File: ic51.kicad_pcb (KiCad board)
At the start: 2 copper layers, 80 x 80 mm, 5 parts, among them J1 Conn_02x18_Odd_Even, J2 Conn_02x18_Odd_Even, J3 Conn_02x18_Odd_Even, J4 Conn_02x18_Odd_Even, U1 ic51-1444-schem

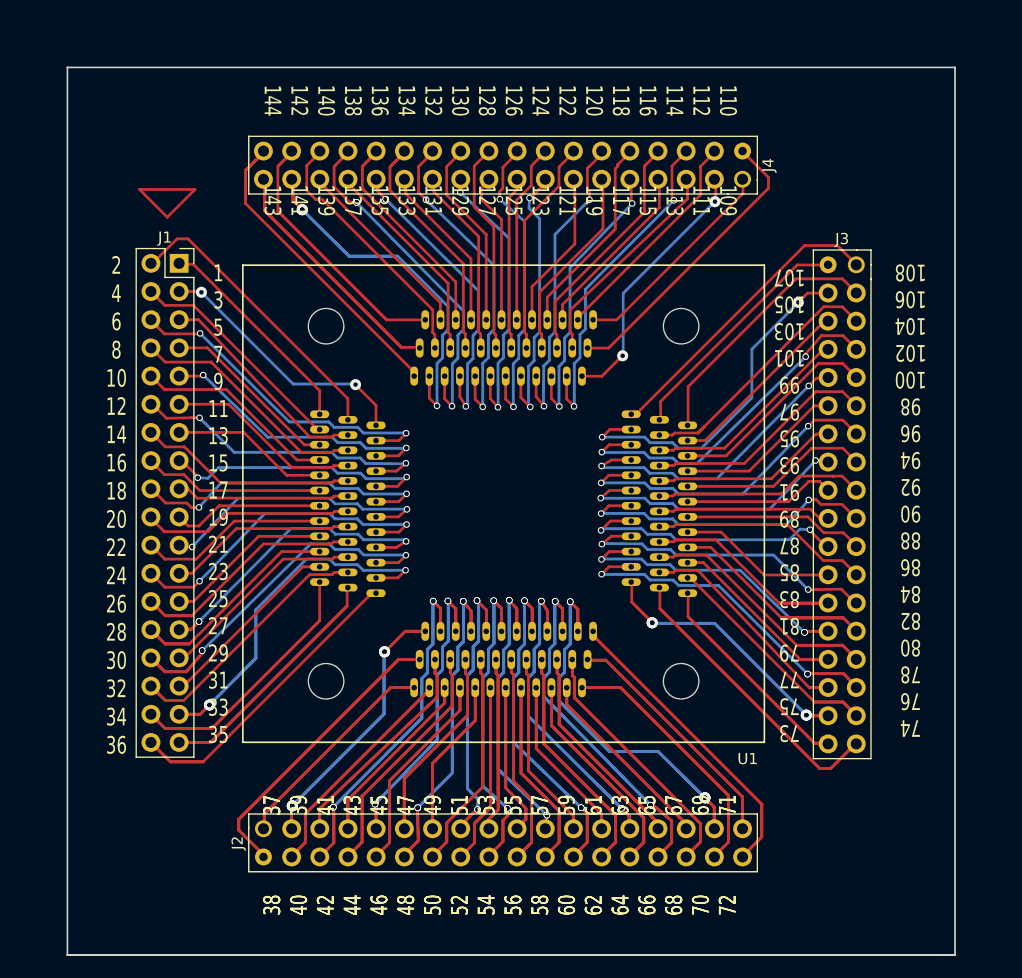
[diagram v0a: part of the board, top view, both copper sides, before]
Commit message: decrease font size og text in F.silk layer
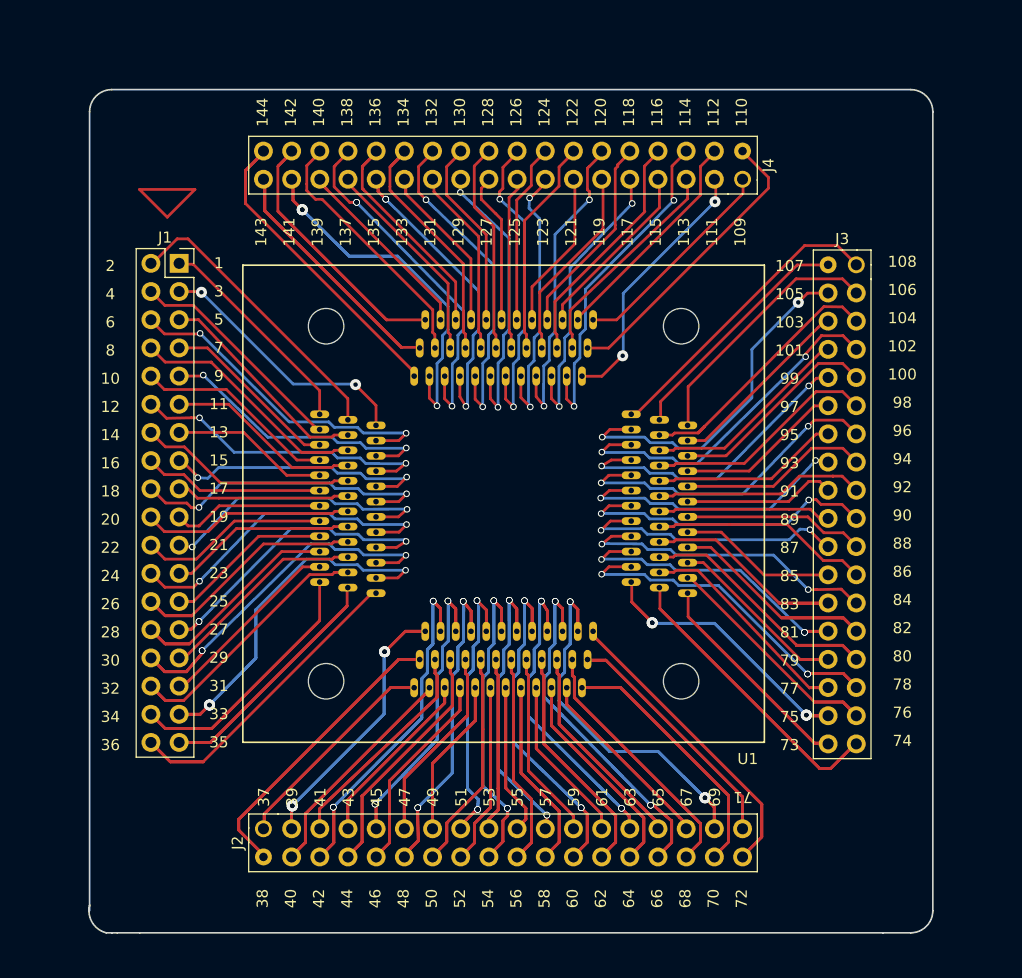
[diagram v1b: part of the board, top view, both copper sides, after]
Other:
- board size 80 x 80 mm -> 76.1 x 76 mm
- board text added: "10"
- board text added: "100"
- board text added: "101"
- board text added: "102"
- board text added: "103"
- board text added: "104"
- board text added: "105"
- board text added: "106"
- board text added: "107"
- board text added: "108"
- board text added: "109"
- board text added: "11"
- board text added: "110"
- board text added: "111"
- board text added: "112"
- board text added: "113"
- board text added: "114"
- board text added: "115"
- board text added: "116"
- board text added: "117"
- board text added: "118"
- board text added: "119"
- board text added: "12"
- board text added: "120"
- board text added: "121"
- board text added: "122"
- board text added: "123"
- board text added: "124"
- board text added: "125"
- board text added: "126"
- board text added: "127"
- board text added: "128"
- board text added: "129"
- board text added: "13"
- board text added: "130"
- board text added: "131"
- board text added: "132"
- board text added: "133"
- board text added: "134"
- board text added: "135"
- board text added: "136"
- board text added: "137"
- board text added: "138"
- board text added: "139"
- board text added: "14"
- board text added: "140"
- board text added: "141"
- board text added: "142"
- board text added: "143"
- board text added: "144"
- board text added: "15"
- board text added: "16"
- board text added: "17"
- board text added: "18"
- board text added: "19"
- board text added: "2"
- board text added: "20"
- board text added: "21"
- board text added: "22"
- board text added: "23"
- board text added: "24"
- board text added: "25"
- board text added: "26"
- board text added: "27"
- board text added: "28"
- board text added: "29"
- board text added: "3"
- board text added: "30"
- board text added: "31"
- board text added: "32"
- board text added: "33"
- board text added: "34"
- board text added: "35"
- board text added: "36"
- board text added: "37"
- board text added: "38"
- board text added: "39"
- board text added: "4"
- board text added: "40"
- board text added: "41"
- board text added: "42"
- board text added: "43"
- board text added: "44"
- board text added: "45"
- board text added: "46"
- board text added: "47"
- board text added: "48"
- board text added: "49"
- board text added: "5"
- board text added: "50"
- board text added: "51"
- board text added: "52"
- board text added: "53"
- board text added: "54"
- board text added: "55"
- board text added: "56"
- board text added: "57"
- board text added: "58"
- board text added: "59"
- board text added: "6"
- board text added: "60"
- board text added: "61"
- board text added: "62"
- board text added: "63"
- board text added: "64"
- board text added: "65"
- board text added: "66"
- board text added: "67"
- board text added: "68"
- board text added: "69"
- board text added: "7"
- board text added: "70"
- board text added: "71"
- board text added: "72"
- board text added: "73"
- board text added: "74"
- board text added: "75"
- board text added: "76"
- board text added: "77"
- board text added: "78"
- board text added: "79"
- board text added: "8"
- board text added: "80"
- board text added: "81"
- board text added: "82"
- board text added: "83"
- board text added: "84"
- board text added: "85"
- board text added: "86"
- board text added: "87"
- board text added: "88"
- board text added: "89"
- board text added: "9"
- board text added: "90"
- board text added: "91"
- board text added: "92"
- board text added: "93"
- board text added: "94"
- board text added: "95"
- board text added: "96"
- board text added: "97"
- board text added: "98"
- board text added: "99"
- board text removed: "1 3 5 7 9 11 13 15 17 19 21 23 25 27 29 31 33 35"
- board text removed: "109 111 113 115 117 119 121 123 125 127 129 131 133 135 137 139 141 143"
- board text removed: "110 112 114 116 118 120 122 124 126 128 130 132 134 136 138 140 142 144"
- board text removed: "2 4 6 8 10 12 14 16 18 20 22 24 26 28 30 32 34 36"
- board text removed: "37 39 41 43 45 47 49 51 53 55 57 59 61 63 65 67 69 71"
- board text removed: "38 40 42 44 46 48 50 52 54 56 58 60 62 64 66 68 70 72"
- board text removed: "73 75 77 79 81 83 85 87 89 91 93 95 97 99 101 103 105 107"
- board text removed: "74 76 78 80 82 84 86 88 90 92 94 96 98 100 102 104 106 108"

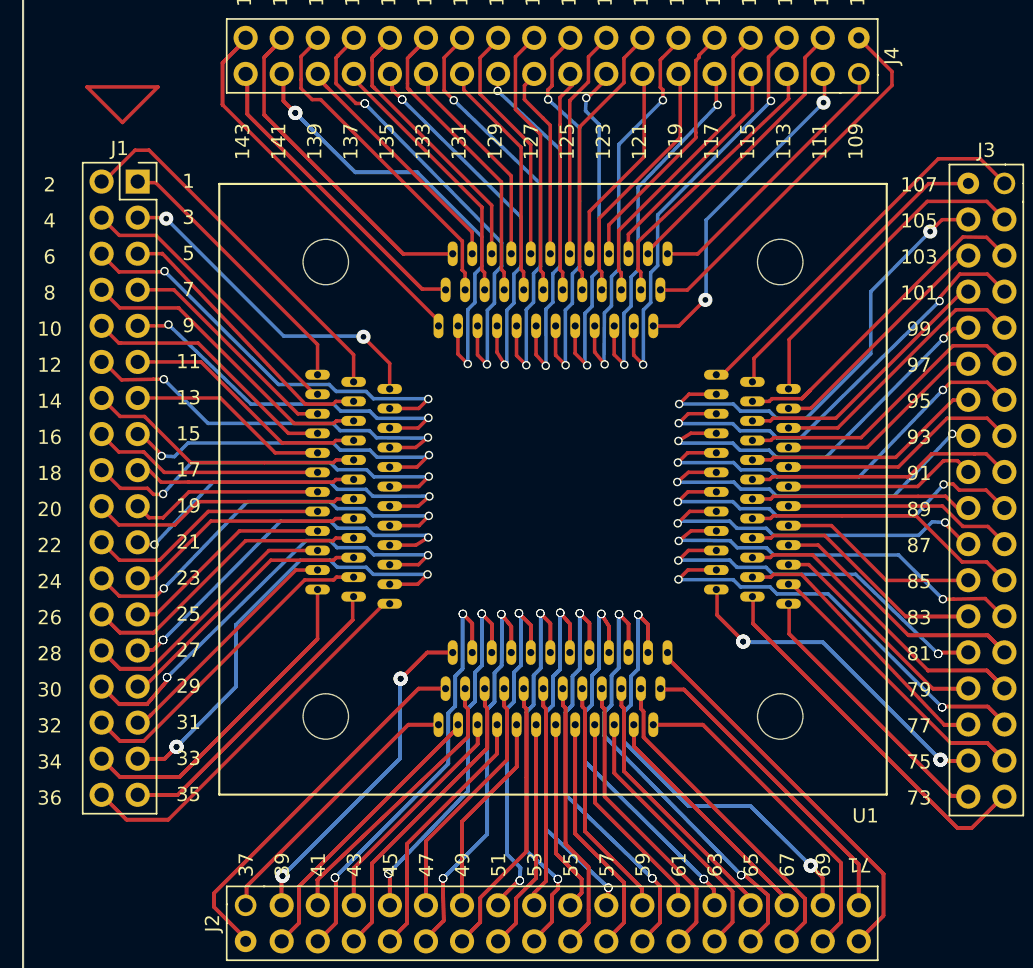
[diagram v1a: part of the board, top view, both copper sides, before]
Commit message: unify all vias to 0.6mm, decrease the size of the triangle
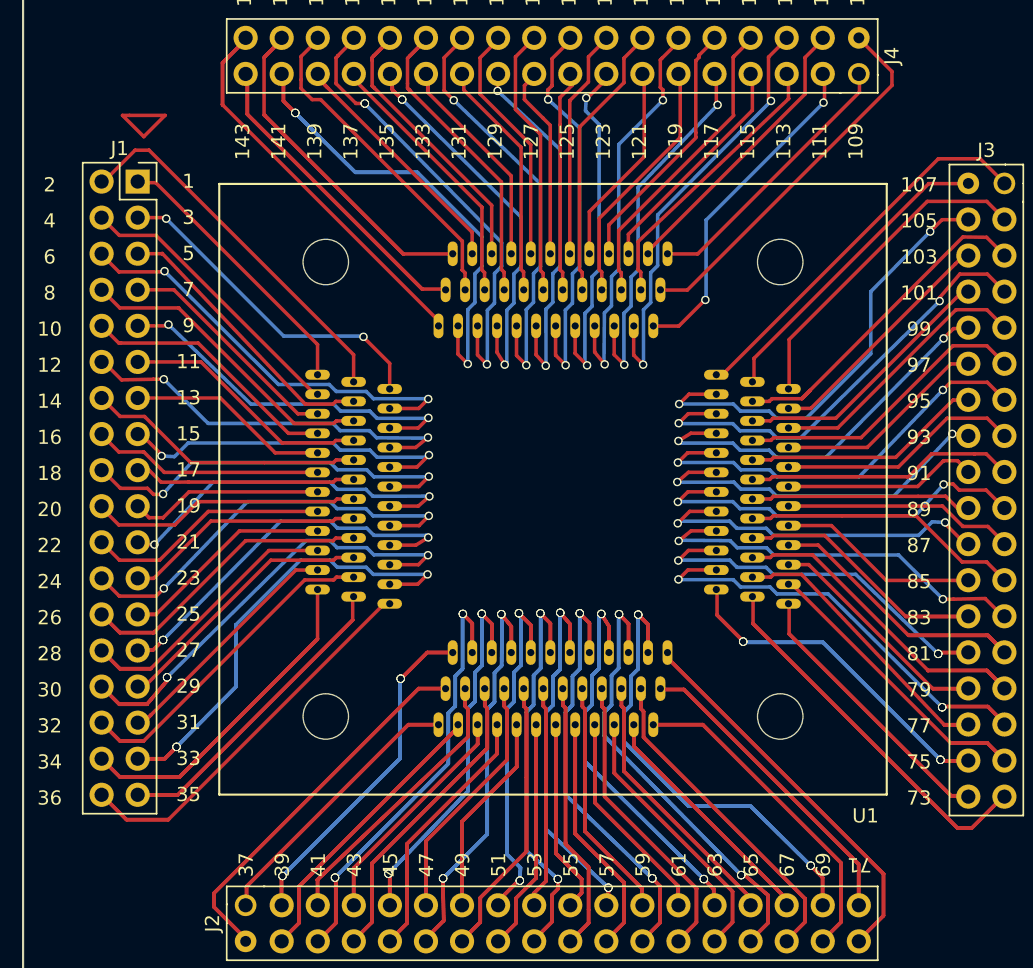
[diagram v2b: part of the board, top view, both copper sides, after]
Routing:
- net (no net): track 13.0 -> 8.14 mm
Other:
- net class Default: via_dia 1 -> 0.6
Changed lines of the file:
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@@
     (links 144)
     (no_connects 0)
-    (area 108.863446 56.424999 185.075001 132.575001)
+    (area -111.414286 -111.414286 213.909502 133.042382)
     (thickness 1.6)
     (drawings 159)
-    (tracks 1567)
+    (tracks 1568)
     (zones 0)
     (modules 5)
@@
     (segment_width 0.2)
     (edge_width 0.15)
-    (via_size 1)
+    (via_size 0.6)
     (via_drill 0.4)
     (via_min_size 0.4)
@@
     (clearance 0.2)
     (trace_width 0.25)
-    (via_dia 1)
+    (via_dia 0.6)
     (via_drill 0.4)
     (uvia_dia 0.3)
@@
     (effects (font (size 1.5 1.5) (thickness 0.3)))
   )
-  (segment (start 113.5 65.5) (end 118.5 65.5) (width 0.25) (layer F.Cu) (net 0))
-  (segment (start 116 68) (end 113.5 65.5) (width 0.25) (layer F.Cu) (net 0))
-  (segment (start 118.5 65.5) (end 116 68) (width 0.25) (layer F.Cu) (net 0))
+  (segment (start 116.5 67.5) (end 119 67.5) (width 0.25) (layer F.Cu) (net 0))
+  (segment (start 116 67.5) (end 116.5 67.5) (width 0.25) (layer F.Cu) (net 0))
+  (segment (start 117.5 69) (end 116 67.5) (width 0.25) (layer F.Cu) (net 0))
+  (segment (start 119 67.5) (end 117.5 69) (width 0.25) (layer F.Cu) (net 0))
   (segment (start 213.5845 97.840999) (end 213.5845 98.3535) (width 0.25) (layer F.Cu) (net 0))
   (segment (start 213.5845 98.2235) (end 213.5845 97.840999) (width 0.25) (layer F.Cu) (net 0))
@@
   (segment (start 119.01 74.7) (end 116.88 74.7) (width 0.25) (layer F.Cu) (net 3))
   (segment (start 119.08 74.77) (end 119.01 74.7) (width 0.25) (layer F.Cu) (net 3))
-  (via (at 119.08 74.77) (size 1) (drill 0.4) (layers F.Cu B.Cu) (net 3))
+  (via (at 119.08 74.77) (size 0.6) (drill 0.4) (layers F.Cu B.Cu) (net 3))
   (segment (start 127.35 83.04) (end 119.08 74.77) (width 0.25) (layer B.Cu) (net 3))
   (segment (start 132.92 83.04) (end 127.35 83.04) (width 0.25) (layer B.Cu) (net 3))
   (segment (start 132.97 83.09) (end 132.92 83.04) (width 0.25) (layer B.Cu) (net 3))
-  (via (at 132.97 83.09) (size 1) (drill 0.4) (layers F.Cu B.Cu) (net 3))
+  (via (at 132.97 83.09) (size 0.6) (drill 0.4) (layers F.Cu B.Cu) (net 3))
   (segment (start 132.97 83.12) (end 132.97 83.09) (width 0.25) (layer F.Cu) (net 3))
   (segment (start 134.815001 84.965001) (end 132.97 83.12) (width 0.25) (layer F.Cu) (net 3))
@@
   (segment (start 118.969841 112.8) (end 119.804894 111.964947) (width 0.25) (layer F.Cu) (net 33))
   (segment (start 116.74 112.8) (end 118.969841 112.8) (width 0.25) (layer F.Cu) (net 33))
-  (via (at 119.804894 111.964947) (size 1) (drill 0.4) (layers F.Cu B.Cu) (net 33))
-  (via (at 119.804894 111.964947) (size 1) (drill 0.4) (layers F.Cu B.Cu) (net 33))
+  (via (at 119.804894 111.964947) (size 0.6) (drill 0.4) (layers F.Cu B.Cu) (net 33))
+  (via (at 119.804894 111.964947) (size 0.6) (drill 0.4) (layers F.Cu B.Cu) (net 33))
   (segment (start 116.74 112.8) (end 118.969841 112.8) (width 0.25) (layer F.Cu) (net 33))
   (segment (start 118.969841 112.8) (end 119.804894 111.964947) (width 0.25) (layer F.Cu) (net 33))
@@
   (segment (start 155.168845 82.335989) (end 157.013846 80.490988) (width 0.25) (layer F.Cu) (net 39))
   (segment (start 157.013846 80.490988) (end 157.043846 80.490988) (width 0.25) (layer F.Cu) (net 39))
-  (via (at 157.043846 80.490988) (size 1) (drill 0.4) (layers F.Cu B.Cu) (net 39))
+  (via (at 157.043846 80.490988) (size 0.6) (drill 0.4) (layers F.Cu B.Cu) (net 39))
   (segment (start 157.043846 80.490988) (end 157.093846 80.440988) (width 0.25) (layer B.Cu) (net 39))
   (segment (start 157.093846 80.440988) (end 157.093846 74.870988) (width 0.25) (layer B.Cu) (net 39))
   (segment (start 157.093846 74.870988) (end 165.363846 66.600988) (width 0.25) (layer B.Cu) (net 39))
-  (via (at 165.363846 66.600988) (size 1) (drill 0.4) (layers F.Cu B.Cu) (net 39))
+  (via (at 165.363846 66.600988) (size 0.6) (drill 0.4) (layers F.Cu B.Cu) (net 39))
   (segment (start 165.363846 66.600988) (end 165.433846 66.530988) (width 0.25) (layer F.Cu) (net 39))
   (segment (start 165.433846 66.530988) (end 165.433846 64.400988) (width 0.25) (layer F.Cu) (net 39))
@@
   (segment (start 127.333846 66.490829) (end 128.168899 67.325882) (width 0.25) (layer F.Cu) (net 69))
   (segment (start 127.333846 64.260988) (end 127.333846 66.490829) (width 0.25) (layer F.Cu) (net 69))
-  (via (at 128.168899 67.325882) (size 1) (drill 0.4) (layers F.Cu B.Cu) (net 69))
-  (via (at 128.168899 67.325882) (size 1) (drill 0.4) (layers F.Cu B.Cu) (net 69))
+  (via (at 128.168899 67.325882) (size 0.6) (drill 0.4) (layers F.Cu B.Cu) (net 69))
+  (via (at 128.168899 67.325882) (size 0.6) (drill 0.4) (layers F.Cu B.Cu) (net 69))
   (segment (start 127.333846 64.260988) (end 127.333846 66.490829) (width 0.25) (layer F.Cu) (net 69))
   (segment (start 127.333846 66.490829) (end 128.168899 67.325882) (width 0.25) (layer F.Cu) (net 69))
@@
   (segment (start 135.615914 107.164782) (end 135.585914 107.164782) (width 0.25) (layer F.Cu) (net 75))
   (segment (start 137.460915 105.319781) (end 135.615914 107.164782) (width 0.25) (layer F.Cu) (net 75))
-  (via (at 135.585914 107.164782) (size 1) (drill 0.4) (layers F.Cu B.Cu) (net 75))
-  (via (at 127.265914 121.054782) (size 1) (drill 0.4) (layers F.Cu B.Cu) (net 75))
+  (via (at 135.585914 107.164782) (size 0.6) (drill 0.4) (layers F.Cu B.Cu) (net 75))
+  (via (at 127.265914 121.054782) (size 0.6) (drill 0.4) (layers F.Cu B.Cu) (net 75))
   (segment (start 137.460915 105.319781) (end 135.615914 107.164782) (width 0.25) (layer F.Cu) (net 75))
   (segment (start 135.615914 107.164782) (end 135.585914 107.164782) (width 0.25) (layer F.Cu) (net 75))
-  (via (at 135.585914 107.164782) (size 1) (drill 0.4) (layers F.Cu B.Cu) (net 75))
+  (via (at 135.585914 107.164782) (size 0.6) (drill 0.4) (layers F.Cu B.Cu) (net 75))
   (segment (start 135.585914 107.164782) (end 135.535914 107.214782) (width 0.25) (layer B.Cu) (net 75))
   (segment (start 135.535914 107.214782) (end 135.535914 112.784782) (width 0.25) (layer B.Cu) (net 75))
   (segment (start 135.535914 112.784782) (end 127.265914 121.054782) (width 0.25) (layer B.Cu) (net 75))
-  (via (at 127.265914 121.054782) (size 1) (drill 0.4) (layers F.Cu B.Cu) (net 75))
+  (via (at 127.265914 121.054782) (size 0.6) (drill 0.4) (layers F.Cu B.Cu) (net 75))
   (segment (start 127.265914 121.054782) (end 127.195914 121.124782) (width 0.25) (layer F.Cu) (net 75))
   (segment (start 127.195914 121.124782) (end 127.195914 123.254782) (width 0.25) (layer F.Cu) (net 75))
@@
   (segment (start 153.008414 103.347282) (end 153.008414 105.319781) (width 0.25) (layer F.Cu) (net 105))
   (via (at 152.315914 102.654782) (size 0.6) (drill 0.4) (layers F.Cu B.Cu) (net 105))
-  (via (at 164.460861 120.329888) (size 1) (drill 0.4) (layers F.Cu B.Cu) (net 105))
+  (via (at 164.460861 120.329888) (size 0.6) (drill 0.4) (layers F.Cu B.Cu) (net 105))
   (segment (start 151.315914 111.604782) (end 151.315914 109.504782) (width 0.25) (layer B.Cu) (net 105))
   (segment (start 151.315914 109.504782) (end 151.815914 109.004782) (width 0.25) (layer B.Cu) (net 105))
@@
   (segment (start 165.295914 121.164941) (end 164.460861 120.329888) (width 0.25) (layer F.Cu) (net 105))
   (segment (start 165.295914 123.394782) (end 165.295914 121.164941) (width 0.25) (layer F.Cu) (net 105))
-  (via (at 164.460861 120.329888) (size 1) (drill 0.4) (layers F.Cu B.Cu) (net 105))
+  (via (at 164.460861 120.329888) (size 0.6) (drill 0.4) (layers F.Cu B.Cu) (net 105))
   (segment (start 156.860913 110.399781) (end 166.585914 120.124782) (width 0.25) (layer F.Cu) (net 106))
   (segment (start 166.585914 124.314782) (end 165.295914 125.604782) (width 0.25) (layer F.Cu) (net 106))
@@
   (segment (start 162.942959 86.75739) (end 162.942959 83.279891) (width 0.25) (layer F.Cu) (net 111))
   (segment (start 176.85796 73.55489) (end 178.14796 74.84489) (width 0.25) (layer F.Cu) (net 111))
-  (via (at 172.873066 75.679943) (size 1) (drill 0.4) (layers F.Cu B.Cu) (net 112))
+  (via (at 172.873066 75.679943) (size 0.6) (drill 0.4) (layers F.Cu B.Cu) (net 112))
   (segment (start 175.93796 74.84489) (end 173.708119 74.84489) (width 0.25) (layer F.Cu) (net 112))
   (segment (start 173.708119 74.84489) (end 172.873066 75.679943) (width 0.25) (layer F.Cu) (net 112))
@@
   (segment (start 159.70796 104.52489) (end 159.70796 104.55489) (width 0.25) (layer F.Cu) (net 142))
   (segment (start 173.66796 112.94489) (end 175.79796 112.94489) (width 0.25) (layer F.Cu) (net 142))
-  (via (at 173.59796 112.87489) (size 1) (drill 0.4) (layers F.Cu B.Cu) (net 142))
-  (via (at 159.70796 104.55489) (size 1) (drill 0.4) (layers F.Cu B.Cu) (net 142))
+  (via (at 173.59796 112.87489) (size 0.6) (drill 0.4) (layers F.Cu B.Cu) (net 142))
+  (via (at 159.70796 104.55489) (size 0.6) (drill 0.4) (layers F.Cu B.Cu) (net 142))
   (segment (start 157.862959 100.88239) (end 157.862959 102.679889) (width 0.25) (layer F.Cu) (net 142))
   (segment (start 173.66796 112.94489) (end 175.79796 112.94489) (width 0.25) (layer F.Cu) (net 142))
   (segment (start 173.59796 112.87489) (end 173.66796 112.94489) (width 0.25) (layer F.Cu) (net 142))
-  (via (at 173.59796 112.87489) (size 1) (drill 0.4) (layers F.Cu B.Cu) (net 142))
+  (via (at 173.59796 112.87489) (size 0.6) (drill 0.4) (layers F.Cu B.Cu) (net 142))
   (segment (start 165.32796 104.60489) (end 173.59796 112.87489) (width 0.25) (layer B.Cu) (net 142))
   (segment (start 159.75796 104.60489) (end 165.32796 104.60489) (width 0.25) (layer B.Cu) (net 142))
   (segment (start 159.70796 104.55489) (end 159.75796 104.60489) (width 0.25) (layer B.Cu) (net 142))
-  (via (at 159.70796 104.55489) (size 1) (drill 0.4) (layers F.Cu B.Cu) (net 142))
+  (via (at 159.70796 104.55489) (size 0.6) (drill 0.4) (layers F.Cu B.Cu) (net 142))
   (segment (start 159.70796 104.52489) (end 159.70796 104.55489) (width 0.25) (layer F.Cu) (net 142))
   (segment (start 157.862959 102.679889) (end 159.70796 104.52489) (width 0.25) (layer F.Cu) (net 142))
